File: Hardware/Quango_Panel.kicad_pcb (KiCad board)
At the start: 2 copper layers, 70.8 x 128.5 mm, 29 parts

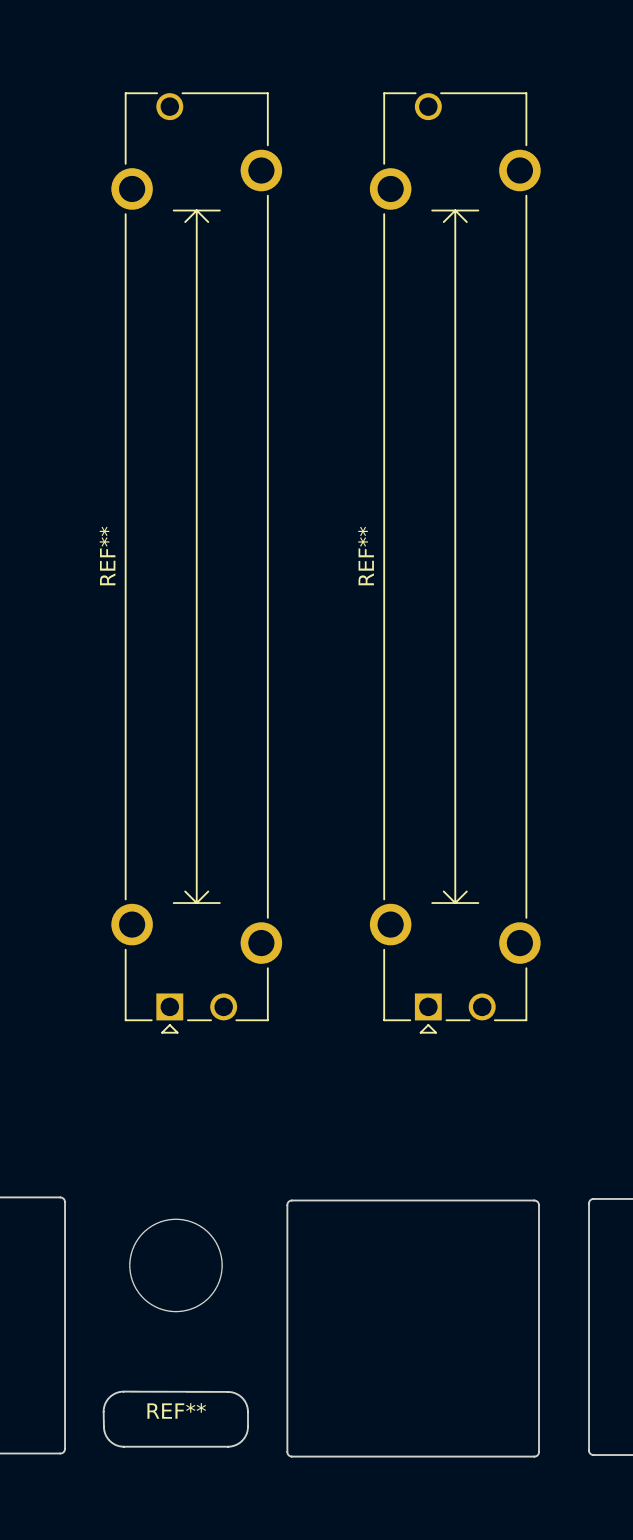
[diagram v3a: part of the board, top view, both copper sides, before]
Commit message: Preparing panel and control board for routing
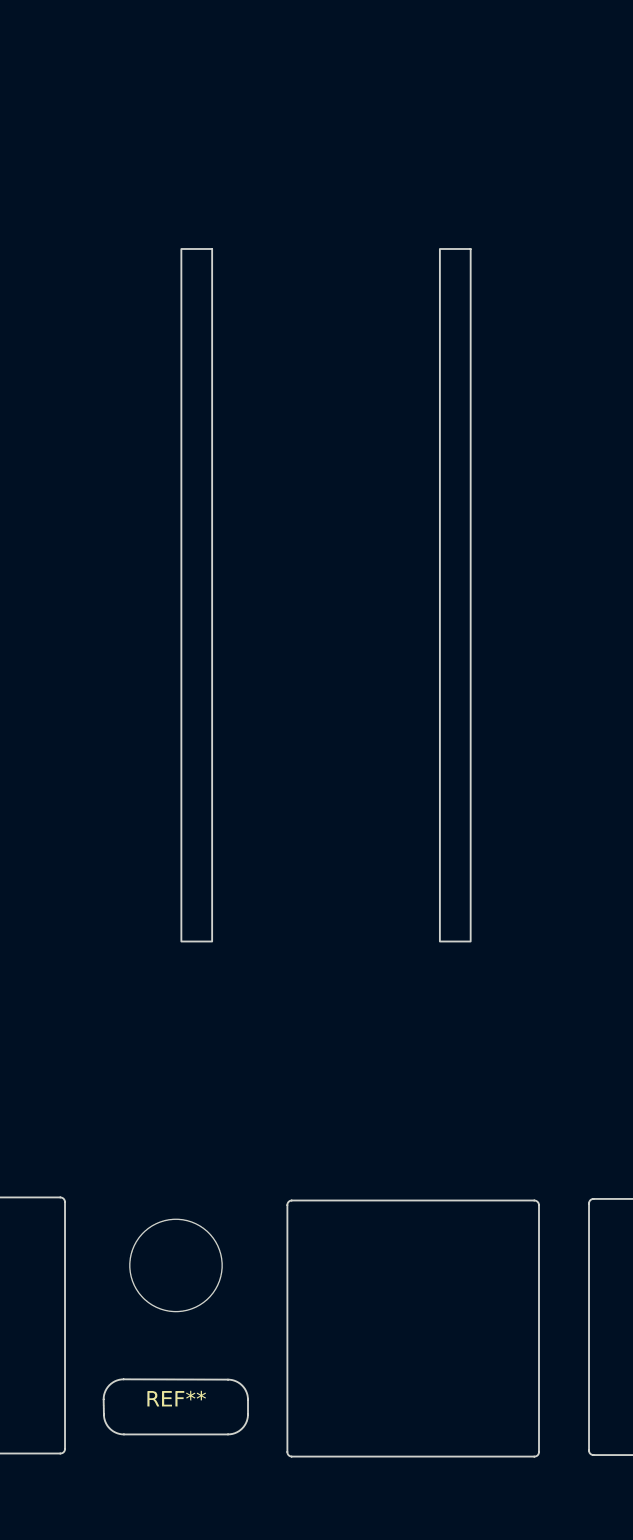
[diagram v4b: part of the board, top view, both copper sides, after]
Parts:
- removed the REF** at (75.2, 118.5)
- removed the REF** at (92.0, 118.5)
- added Level1: 10k, Custom_Footprints:Potentiometer_Bourns_PTA4543_Slot, F.Cu at (78.7, 62.5)
- added Level1: 10k, Custom_Footprints:Potentiometer_Bourns_PTA4543_Slot, F.Cu at (95.5, 62.5)
- moved REF** 0.80 mm to (75.6, 144.5)

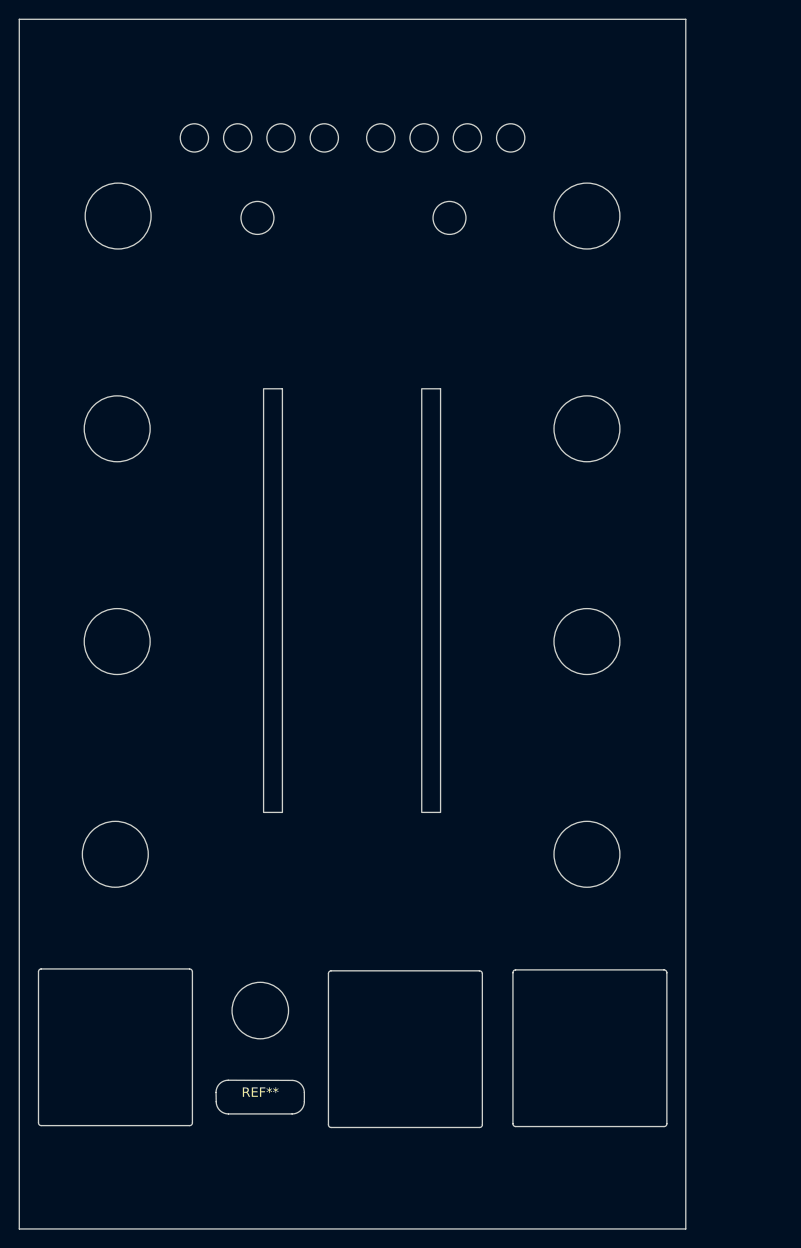
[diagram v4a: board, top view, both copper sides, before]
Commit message: First draft routing of control board
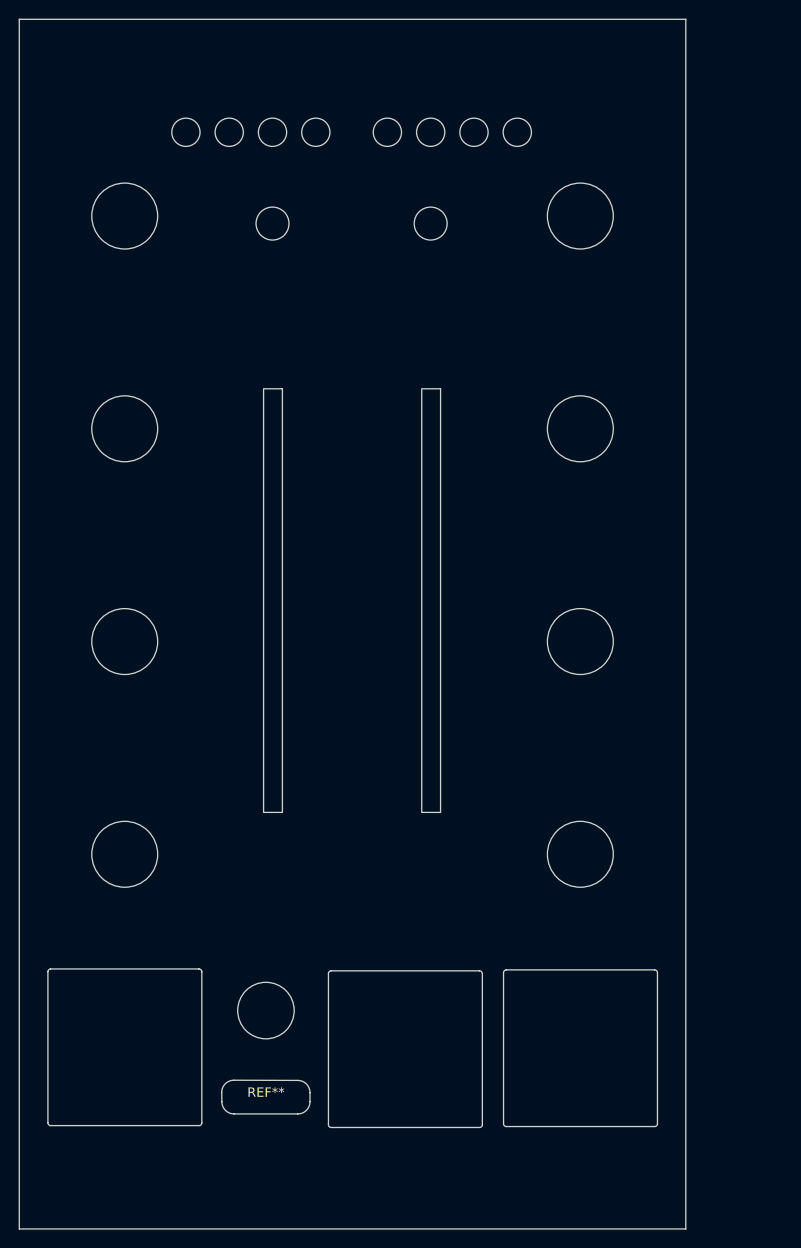
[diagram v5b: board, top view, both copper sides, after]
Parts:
- moved RESET 2.09 mm to (93.7, 51.7)
- moved RESET 1.71 mm to (76.9, 51.7)
- moved Ref** 1.08 mm to (72.3, 42.0)
- moved Ref** 1.08 mm to (81.5, 42.0)
- moved Ref** 1.08 mm to (76.9, 42.0)
- moved Ref** 1.08 mm to (67.7, 42.0)
- moved REF** 1.00 mm to (61.2, 139.2)
- moved REF** 1.00 mm to (109.6, 139.3)
- moved Ref** 1.00 mm to (61.2, 118.7)
- moved Ref** 0.92 mm to (98.3, 42.0)
- moved Ref** 0.92 mm to (102.9, 42.0)
- moved Ref** 0.92 mm to (93.7, 42.0)
- moved Ref** 0.92 mm to (89.1, 42.0)
- moved Ref** 0.80 mm to (61.2, 96.1)
- moved Ref** 0.80 mm to (61.2, 73.5)
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
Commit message: Added Gate ouputs to component board
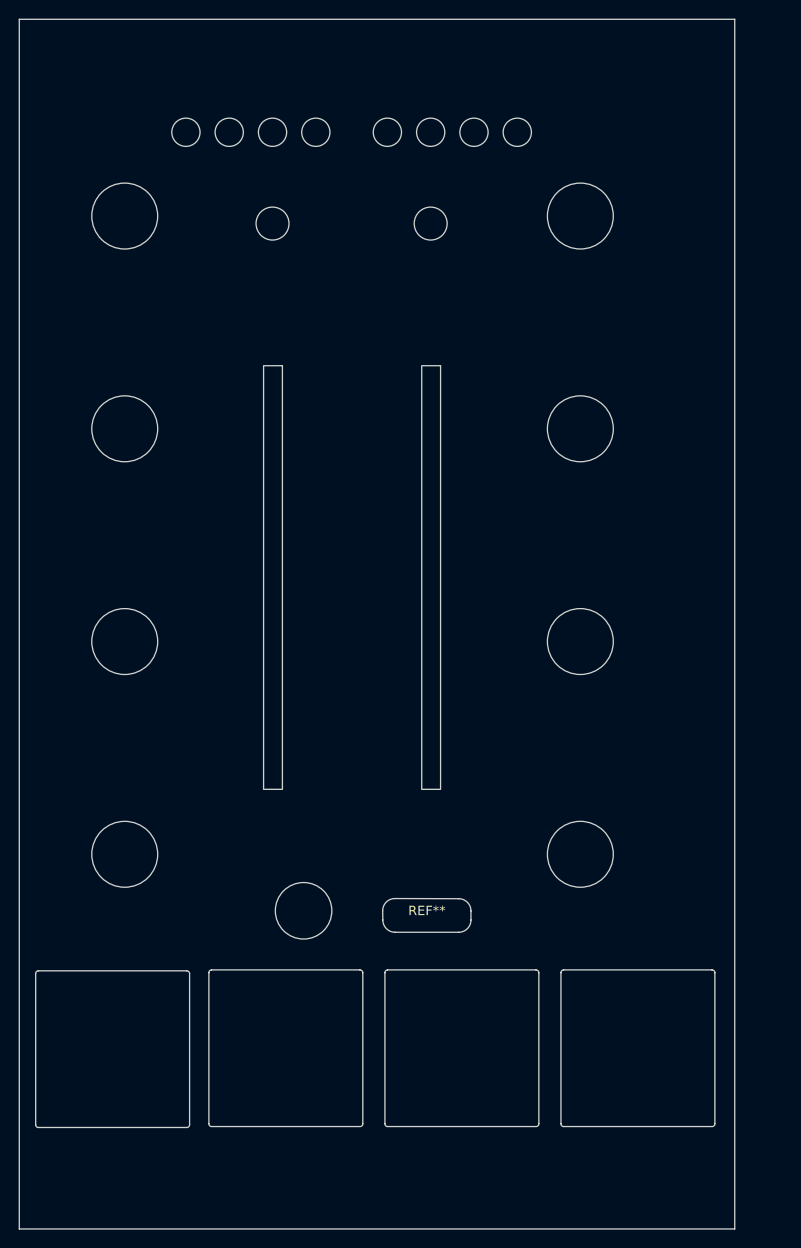
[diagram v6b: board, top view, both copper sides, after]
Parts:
- added REF**: RJ45_Molex_42878-8506_Mounting_Hole, Custom_Footprints:RJ45_Molex_42878-8506_Mounting_Hole, F.Cu at (78.3, 139.3)
- moved REF** 25.8 mm to (93.3, 125.2)
- moved Ref** 11.3 mm to (80.2, 124.7)
- moved REF** 6.10 mm to (115.7, 139.3)
- moved REF** 6.00 mm to (97.0, 139.3)
- moved Level1 2.45 mm to (78.7, 60.0)
- moved Level1 2.45 mm to (95.5, 60.0)
- moved REF** 1.32 mm to (59.9, 139.4)
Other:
- board size 70.8 x 128.5 mm -> 76 x 128.5 mm
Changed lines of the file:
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@@
   )
   (footprint "Custom_Footprints:RJ45_Molex_42878-8506_Mounting_Hole" (layer "F.Cu")
-    (at 61.2 139.2)
+    (at 59.9 139.4)
     (descr "RJ45 vertical connector https://www.on-shore.com/wp-content/uploads/PJ012-8P8CX.pdf")
     (tags "RJ45 PJ012")
@@
     (fp_arc (start -7.88 8.32) (mid -8.081749 8.227632) (end -8.16 8.02) (layer "Edge.Cuts") (width 0.12))
     (fp_arc (start -8.16 -8.02) (mid -8.081443 -8.227347) (end -7.88 -8.32) (layer "Edge.Cuts") (width 0.12))
-    (fp_arc (start 7.88 -8.32) (mid 8.096588 -8.233658) (end 8.19 -8.02) (layer "Edge.Cuts") (width 0.12))
+    (fp_arc (start 7.88 -8.32) (mid 8.096622 -8.233665) (end 8.19 -8.02) (layer "Edge.Cuts") (width 0.12))
     (fp_arc (start 8.19 8.02) (mid 8.100917 8.238111) (end 7.88 8.32) (layer "Edge.Cuts") (width 0.12))
     (fp_line (start -8.31 -8.5) (end 8.39 -8.5) (layer "F.CrtYd") (width 0.05))
@@
   )
   (footprint "Custom_Footprints:RJ45_Molex_42878-8506_Mounting_Hole" (layer "F.Cu")
-    (at 91 139.4)
+    (at 97 139.3)
     (descr "RJ45 vertical connector https://www.on-shore.com/wp-content/uploads/PJ012-8P8CX.pdf")
     (tags "RJ45 PJ012")
@@
     (fp_line (start 8.19 -8.02) (end 8.19 8.02) (layer "Edge.Cuts") (width 0.12))
     (fp_line (start 7.88 -8.32) (end -7.88 -8.32) (layer "Edge.Cuts") (width 0.12))
-    (fp_arc (start 7.88 -8.32) (mid 8.096588 -8.233658) (end 8.19 -8.02) (layer "Edge.Cuts") (width 0.12))
+    (fp_arc (start 7.88 -8.32) (mid 8.096622 -8.233665) (end 8.19 -8.02) (layer "Edge.Cuts") (width 0.12))
     (fp_arc (start -8.16 -8.02) (mid -8.081443 -8.227347) (end -7.88 -8.32) (layer "Edge.Cuts") (width 0.12))
     (fp_arc (start -7.88 8.32) (mid -8.081749 8.227632) (end -8.16 8.02) (layer "Edge.Cuts") (width 0.12))
@@
   )
   (footprint "Custom_Footprints:Thonkiconn_Socket_MountingHole_6mm" (layer "F.Cu")
-    (at 76.2 135.3)
+    (at 80.2 124.7)
     (descr "Mounting Hole 6mm, no annular")
     (tags "mounting hole 6mm no annular")
@@
   )
   (footprint "Custom_Footprints:USB_C_Cutout" (layer "F.Cu")
-    (at 76.2 144.5)
+    (at 93.3 125.2)
     (attr smd)
     (fp_text reference "REF**" (at 0 -0.5 unlocked) (layer "F.SilkS")
@@
   )
   (footprint "Custom_Footprints:RJ45_Molex_42878-8506_Mounting_Hole" (layer "F.Cu")
-    (at 109.6 139.3)
+    (at 115.7 139.3)
     (descr "RJ45 vertical connector https://www.on-shore.com/wp-content/uploads/PJ012-8P8CX.pdf")
     (tags "RJ45 PJ012")
@@
     (fp_arc (start 8.19 8.02) (mid 8.100917 8.238111) (end 7.88 8.32) (layer "Edge.Cuts") (width 0.12))
     (fp_arc (start -7.88 8.32) (mid -8.081749 8.227632) (end -8.16 8.02) (layer "Edge.Cuts") (width 0.12))
-    (fp_arc (start 7.88 -8.32) (mid 8.096588 -8.233658) (end 8.19 -8.02) (layer "Edge.Cuts") (width 0.12))
+    (fp_arc (start 7.88 -8.32) (mid 8.096622 -8.233665) (end 8.19 -8.02) (layer "Edge.Cuts") (width 0.12))
     (fp_line (start -8.31 -8.5) (end 8.39 -8.5) (layer "F.CrtYd") (width 0.05))
     (fp_line (start 8.39 -8.5) (end 8.39 8.5) (layer "F.CrtYd") (width 0.05))
@@
   )
   (footprint "Custom_Footprints:Potentiometer_Bourns_PTA4543_Slot" (layer "F.Cu")
-    (at 78.7 62.5 -90)
+    (at 78.7 60.05 -90)
     (descr "Bourns single-gang slide potentiometer, 45.0mm travel, https://www.bourns.com/docs/Product-Datasheets/pta.pdf")
     (tags "Bourns single-gang slide potentiometer 45.0mm")
@@
   )
   (footprint "Custom_Footprints:Potentiometer_Bourns_PTA4543_Slot" (layer "F.Cu")
-    (at 95.5 62.5 -90)
+    (at 95.5 60.05 -90)
     (descr "Bourns single-gang slide potentiometer, 45.0mm travel, https://www.bourns.com/docs/Product-Datasheets/pta.pdf")
     (tags "Bourns single-gang slide potentiometer 45.0mm")
@@
     )
   )
+  (footprint "Custom_Footprints:RJ45_Molex_42878-8506_Mounting_Hole" (layer "F.Cu")
+    (at 78.3 139.3)
+    (descr "RJ45 vertical connector https://www.on-shore.com/wp-content/uploads/PJ012-8P8CX.pdf")
+    (tags "RJ45 PJ012")
+    (attr through_hole)
+    (fp_text reference "REF**" (at 0 10.1) (layer "F.SilkS") hide
+      (effects (font (size 1 1) (thickness 0.15)))
+    )
+    (fp_text value "RJ45_Molex_42878-8506_Mounting_Hole" (at -0.01 -10.5) (layer "F.Fab")
+      (effects (font (size 1 1) (thickness 0.15)))
+    )
+    (fp_text user "${REFERENCE}" (at 0.11 10.05) (layer "F.Fab") hide
+      (effects (font (size 1 1) (thickness 0.15)))
+    )
+    (fp_line (start 7.88 8.32) (end -7.88 8.32) (layer "Edge.Cuts") (width 0.12))
+    (fp_line (start -8.16 -8.02) (end -8.16 8.02) (layer "Edge.Cuts") (width 0.12))
+    (fp_line (start 8.19 -8.02) (end 8.19 8.02) (layer "Edge.Cuts") (width 0.12))
+    (fp_line (start 7.88 -8.32) (end -7.88 -8.32) (layer "Edge.Cuts") (width 0.12))
+    (fp_arc (start 7.88 -8.32) (mid 8.096622 -8.233665) (end 8.19 -8.02) (layer "Edge.Cuts") (width 0.12))
+    (fp_arc (start -8.16 -8.02) (mid -8.081443 -8.227347) (end -7.88 -8.32) (layer "Edge.Cuts") (width 0.12))
+    (fp_arc (start -7.88 8.32) (mid -8.081749 8.227632) (end -8.16 8.02) (layer "Edge.Cuts") (width 0.12))
+    (fp_arc (start 8.19 8.02) (mid 8.100917 8.238111) (end 7.88 8.32) (layer "Edge.Cuts") (width 0.12))
+    (fp_line (start -8.31 8.5) (end 8.39 8.5) (layer "F.CrtYd") (width 0.05))
+    (fp_line (start -8.31 -8.5) (end -8.31 8.5) (layer "F.CrtYd") (width 0.05))
+    (fp_line (start 8.39 -8.5) (end 8.39 8.5) (layer "F.CrtYd") (width 0.05))
+    (fp_line (start -8.31 -8.5) (end 8.39 -8.5) (layer "F.CrtYd") (width 0.05))
+    (model "${CUSTOM_3D}/428788506.stp"
+      (offset (xyz 0.06 -0.3 -5))
+      (scale (xyz 1 1 1))
+      (rotate (xyz 90 -180 90))
+    )
+  )
   (footprint "Custom_Footprints:Small_Pushbutton_Hole_3.5mm" (layer "B.Cu")
     (at 76.9 51.7)
@@
   (gr_rect locked (start 50.1 39) (end 120.7 149) (layer "Dwgs.User") (width 0.15) (fill none))
   (gr_line locked (start 85.4 29) (end 85.4 160.6) (layer "Dwgs.User") (width 0.15))
-  (gr_rect locked (start 50 30) (end 120.8 158.5) (layer "Edge.Cuts") (width 0.1) (fill none))
+  (gr_rect locked (start 50 30) (end 126 158.5) (layer "Edge.Cuts") (width 0.1) (fill none))
 )
